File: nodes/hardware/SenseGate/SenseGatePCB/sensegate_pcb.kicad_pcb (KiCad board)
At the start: 2 copper layers, 110.1 x 110.1 mm, 0 parts

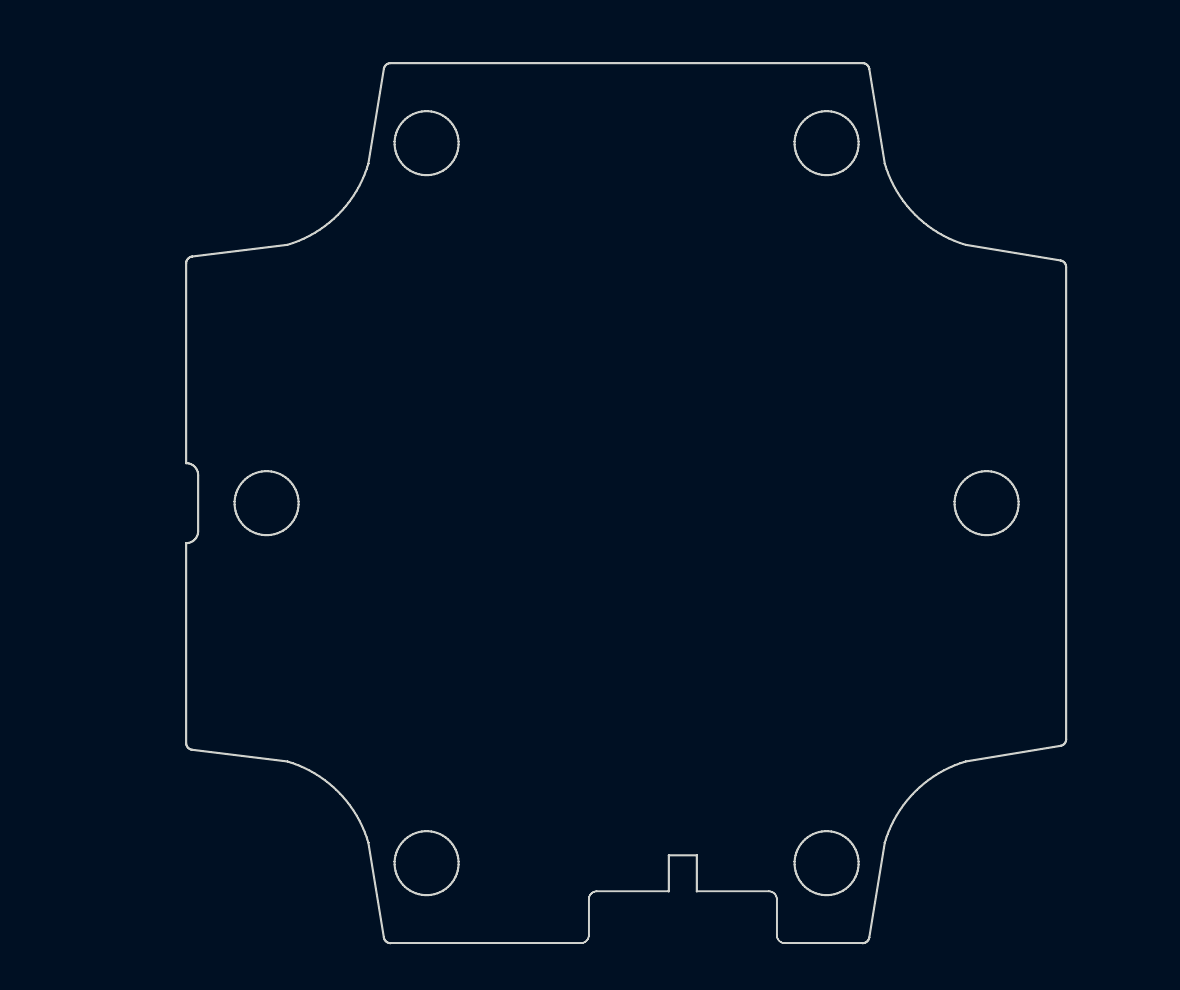
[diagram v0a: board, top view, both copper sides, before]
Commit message: added footprint with pads of sensemate to sensegate pcb
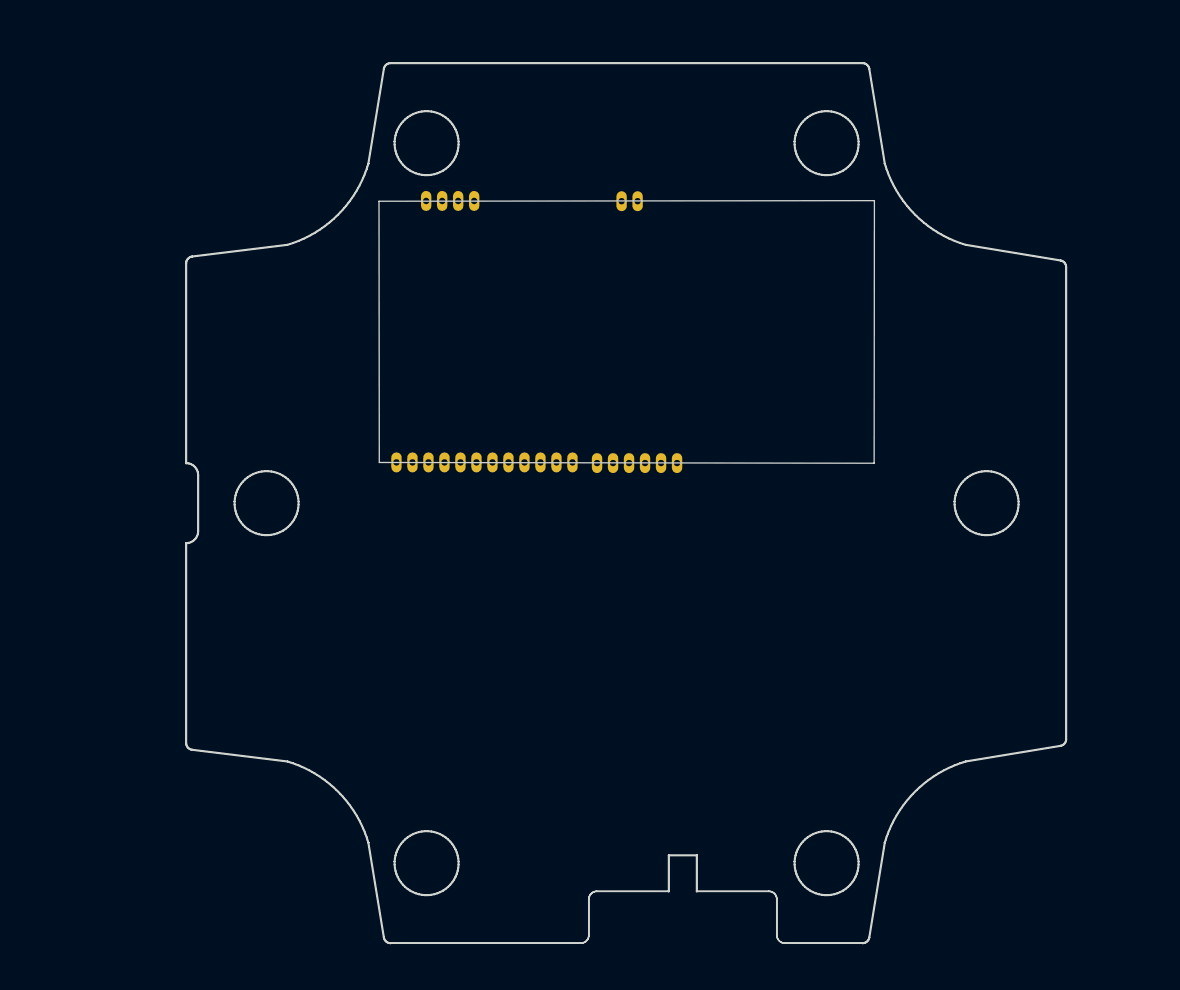
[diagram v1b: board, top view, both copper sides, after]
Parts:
- added J4: Conn_01x24_Pin, SenseGateLib:SenseMateInterface, F.Cu at (122.3, 54.5)

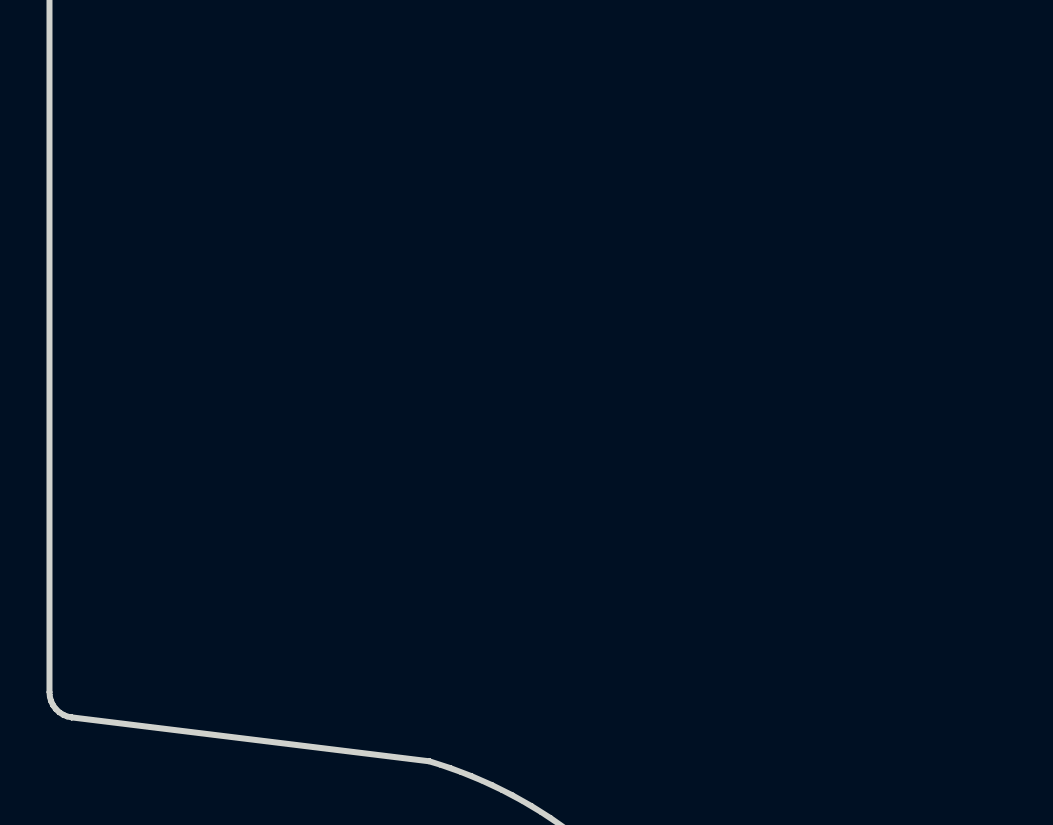
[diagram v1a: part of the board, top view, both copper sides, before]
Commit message: added solar boost converter footprint
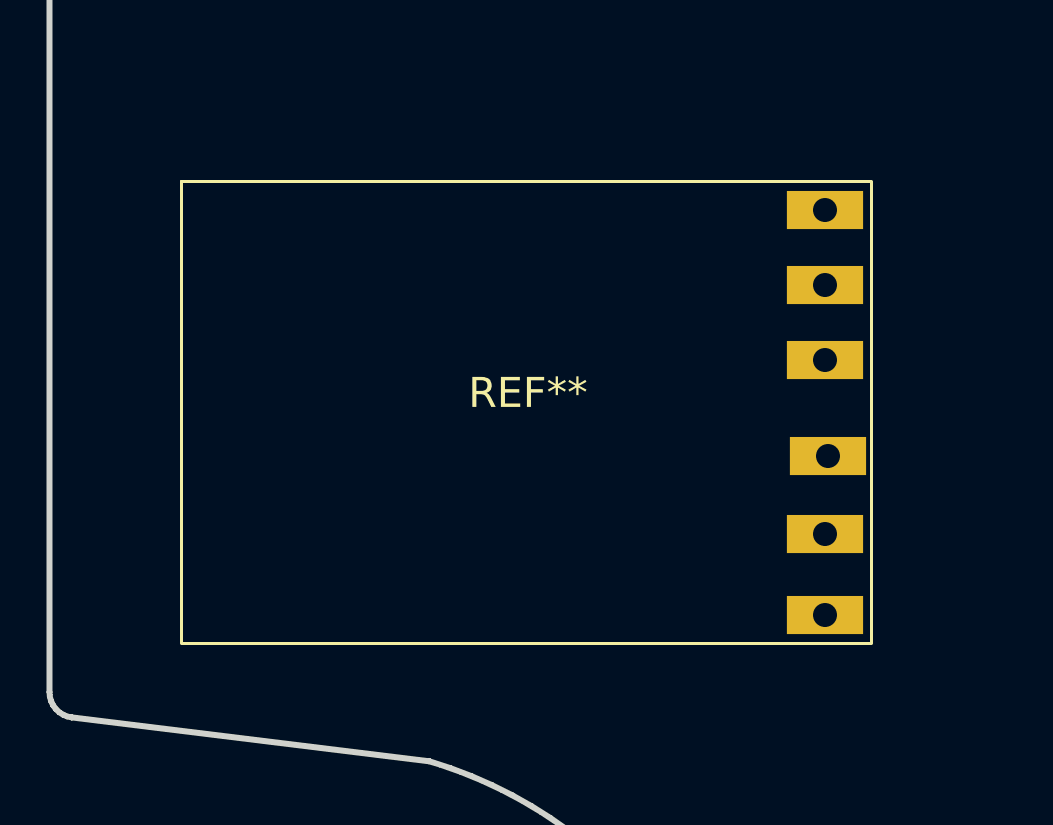
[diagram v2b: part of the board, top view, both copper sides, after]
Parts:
- added REF**: DD05CVSA, custom_dcdc_converters:DD05CVSA, F.Cu at (88.5, 114.5)
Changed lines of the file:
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@@
+		(embedded_fonts no)
+	)
+	(footprint "custom_dcdc_converters:DD05CVSA"
+		(layer "F.Cu")
+		(at 88.5 114.5)
+		(property "Reference" "REF**"
+			(at 0 -0.5 0)
+			(unlocked yes)
+			(layer "F.SilkS")
+			(effects
+				(font
+					(size 1 1)
+					(thickness 0.1)
+				)
+			)
+		)
+		(property "Value" "DD05CVSA"
+			(at 0 1 0)
+			(unlocked yes)
+			(layer "F.Fab")
+			(effects
+				(font
+					(size 1 1)
+					(thickness 0.15)
+				)
+			)
+		)
+		(property "Datasheet" ""
+			(at 0 0 0)
+			(unlocked yes)
+			(layer "F.Fab")
+			(hide yes)
+			(effects
+				(font
+					(size 1 1)
+					(thickness 0.15)
+				)
+			)
+		)
+		(property "Description" ""
+			(at 0 0 0)
+			(unlocked yes)
+			(layer "F.Fab")
+			(hide yes)
+			(effects
+				(font
+					(size 1 1)
+					(thickness 0.15)
+				)
+			)
+		)
+		(attr smd)
+		(duplicate_pad_numbers_are_jumpers no)
+		(fp_rect
+			(start -11.549748 -7.550756)
+			(end 11.450252 7.849244)
+			(stroke
+				(width 0.1)
+				(type default)
+			)
+			(fill no)
+			(layer "F.SilkS")
+		)
+		(fp_rect
+			(start -12 -8)
+			(end 11.9 8.3)
+			(stroke
+				(width 0.05)
+				(type default)
+			)
+			(fill no)
+			(layer "F.CrtYd")
+		)
+		(fp_text user "${REFERENCE}"
+			(at 0 2.5 0)
+			(unlocked yes)
+			(layer "F.Fab")
+			(effects
+				(font
+					(size 1 1)
+					(thickness 0.15)
+				)
+			)
+		)
+		(pad "1" thru_hole rect
+			(at 9.9 -6.6)
+			(size 2.54 1.27)
+			(drill 0.8)
+			(layers "*.Cu" "*.Mask")
+			(remove_unused_layers no)
+		)
+		(pad "2" thru_hole rect
+			(at 9.9 -4.1)
+			(size 2.54 1.27)
+			(drill 0.8)
+			(layers "*.Cu" "*.Mask")
+			(remove_unused_layers no)
+		)
+		(pad "3" thru_hole rect
+			(at 9.9 -1.6)
+			(size 2.54 1.27)
+			(drill 0.8)
+			(layers "*.Cu" "*.Mask")
+			(remove_unused_layers no)
+		)
+		(pad "4" thru_hole rect
+			(at 10 1.6)
+			(size 2.54 1.27)
+			(drill 0.8)
+			(layers "*.Cu" "*.Mask")
+			(remove_unused_layers no)
+		)
+		(pad "5" thru_hole rect
+			(at 9.9 4.2)
+			(size 2.54 1.27)
+			(drill 0.8)
+			(layers "*.Cu" "*.Mask")
+			(remove_unused_layers no)
+		)
+		(pad "6" thru_hole rect
+			(at 9.9 6.9)
+			(size 2.54 1.27)
+			(drill 0.8)
+			(layers "*.Cu" "*.Mask")
+			(remove_unused_layers no)
+		)
 		(embedded_fonts no)
 	)

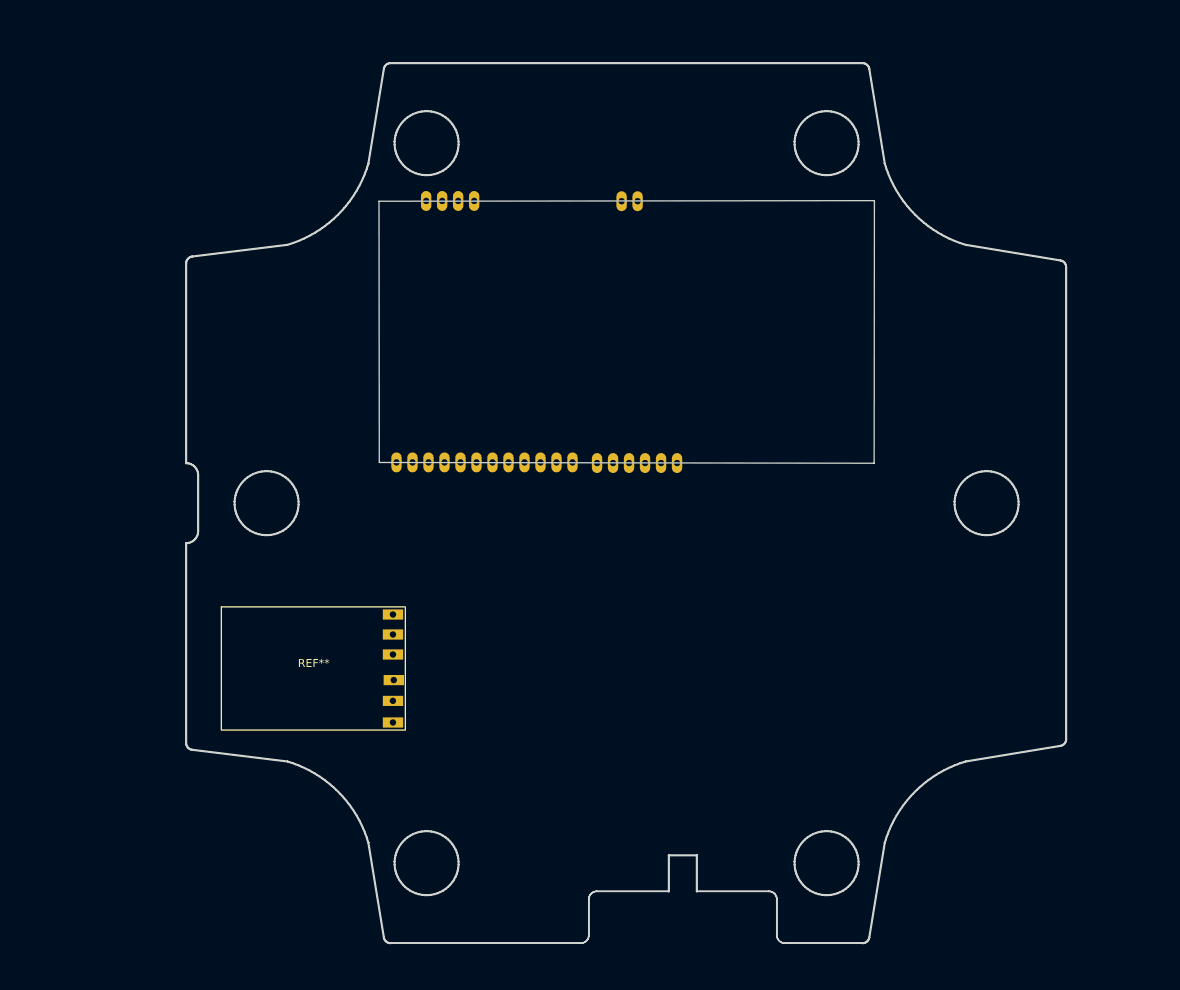
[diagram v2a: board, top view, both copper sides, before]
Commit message: added battery holder, jst terminals, and dcdc for inductive sensor
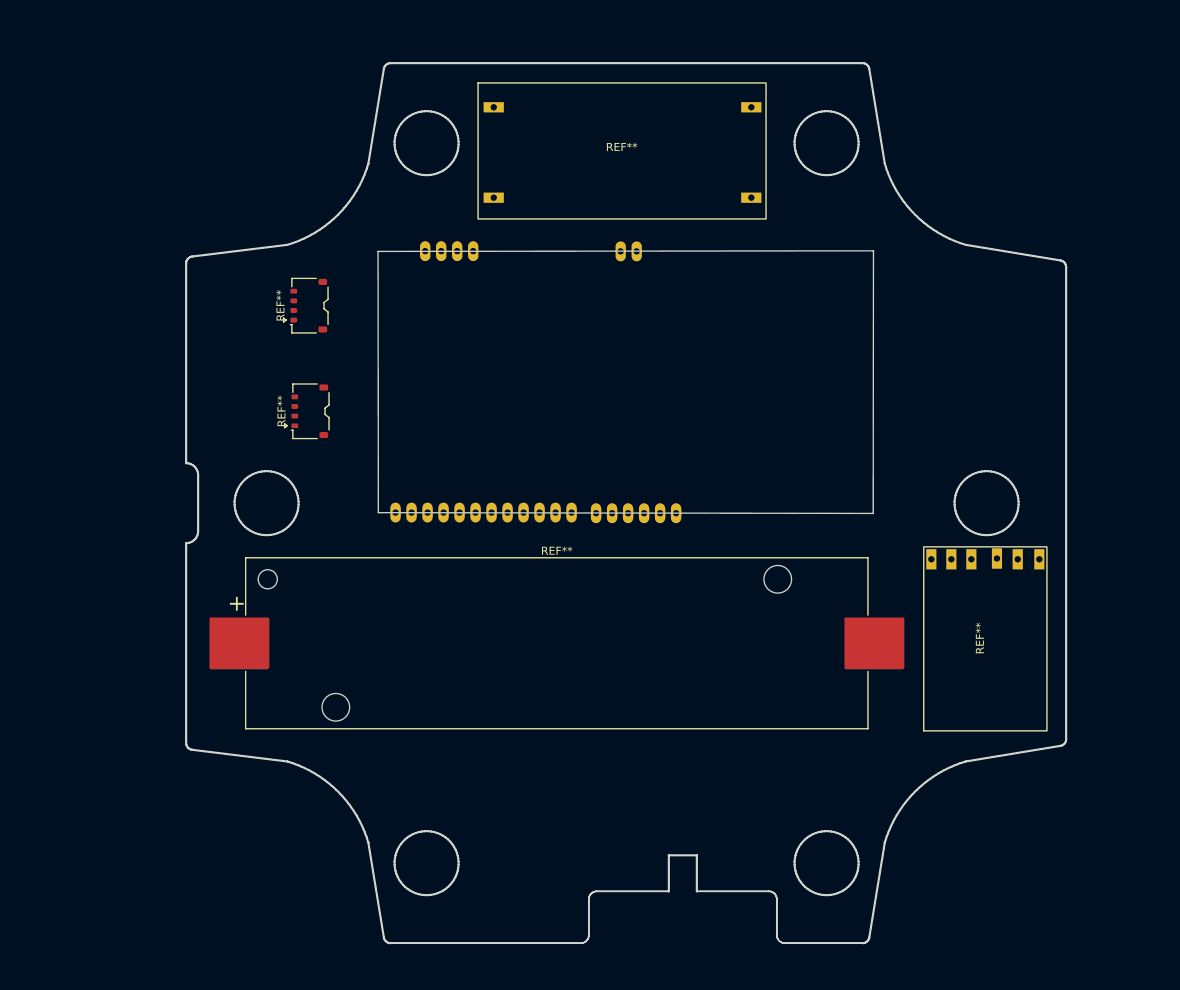
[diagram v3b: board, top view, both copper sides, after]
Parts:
- added REF**: JST_ACH_BM04B-ACHSS-A-GAN-ETF_1x04-1MP_P1.20mm_Vertical, Connector_JST:JST_ACH_BM04B-ACHSS-A-GAN-ETF_1x04-1MP_P1.20mm_Vertical, F.Cu at (87.9, 69.3)
- added REF**: BatteryHolder_Keystone_1042_1x18650, Battery:BatteryHolder_Keystone_1042_1x18650, F.Cu at (118.9, 111.5)
- added REF**: Solarbotics, custom_dcdc_converters:Solarbotics, F.Cu at (127.0, 50.0)
- added REF**: JST_ACH_BM04B-ACHSS-A-GAN-ETF_1x04-1MP_P1.20mm_Vertical, Connector_JST:JST_ACH_BM04B-ACHSS-A-GAN-ETF_1x04-1MP_P1.20mm_Vertical, F.Cu at (88.0, 82.5)
- moved REF** 83.9 mm to (172.3, 110.9), turned to 90 degrees
- moved J4 6.27 mm to (122.2, 60.8)

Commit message: wip schematic and pcb
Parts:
- removed REF** (x2): JST_ACH_BM04B-ACHSS-A-GAN-ETF_1x04-1MP_P1.20mm_Vertical, Connector_JST:JST_ACH_BM04B-ACHSS-A-GAN-ETF_1x04-1MP_P1.20mm_Vertical
- removed REF**: DD05CVSA, custom_dcdc_converters:DD05CVSA
- removed REF**: BatteryHolder_Keystone_1042_1x18650, Battery:BatteryHolder_Keystone_1042_1x18650
- removed REF**: Solarbotics, custom_dcdc_converters:Solarbotics
- added J5: Conn_01x04_Socket, Connector_JST:JST_PH_B4B-PH-K_1x04_P2.00mm_Vertical, F.Cu at (89.7, 106.1)
- added J6: Conn_01x04_Socket, Connector_JST:JST_PH_B4B-PH-K_1x04_P2.00mm_Vertical, F.Cu at (110.5, 108.9)
- added J7: Conn_01x04_Socket, Connector_JST:JST_PH_B4B-PH-K_1x04_P2.00mm_Vertical, F.Cu at (110.5, 115.5)
- added J8: Conn_01x04_Socket, Connector_JST:JST_PH_B4B-PH-K_1x04_P2.00mm_Vertical, F.Cu at (110.5, 122.0)
- added U1: DD05CVSA, custom_dcdc_converters:DD05CVSA, F.Cu at (171.4, 76.2)
- moved J4 0.14 mm to (122.3, 60.7)
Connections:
- J4 pad +3V3: (no net) -> unconnected-(J4-Pin_21-Pad+3V3)
- J4 pad Battery: (no net) -> unconnected-(J4-Pin_23-PadBattery)
- J4 pad GND: (no net) -> unconnected-(J4-Pin_16-PadGND)
- J4 pad P0.31_D16: (no net) -> unconnected-(J4-Pin_12-PadP0.31_D16)
- J4 pad VBAT: (no net) -> unconnected-(J4-Pin_24-PadVBAT)
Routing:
- added copper zone on F.Cu, net (none)

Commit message: sensegate pcb wip
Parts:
- added BT2: Battery, Connector_JST:JST_PH_S2B-PH-K_1x02_P2.00mm_Horizontal, F.Cu at (156.5, 100.3)
- added Q4: SS8050, Package_TO_SOT_SMD:SOT-23, F.Cu at (136.9, 117.5)
- added R3: R, Resistor_SMD:R_0805_2012Metric, F.Cu at (136.7, 121.2)
- moved U1 49.3 mm to (150.8, 120.9), turned to 90 degrees
- moved J8 19.5 mm to (118.5, 104.3), turned to 90 degrees
- moved J7 11.3 mm to (112.3, 104.3), turned to 90 degrees
- moved J5 10.2 mm to (99.7, 104.2), turned to 90 degrees
- moved J6 6.58 mm to (105.9, 104.2), turned to 90 degrees
- moved J4 5.27 mm to (123.1, 55.5)
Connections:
- J4 pad +3V3: unconnected-(J4-Pin_21-Pad+3V3) -> +3V3
- J4 pad GND: unconnected-(J4-Pin_16-PadGND) -> GND
- J4 pad VBAT: unconnected-(J4-Pin_24-PadVBAT) -> VBAT
- J5 pad 1: testt -> unconnected-(J5-Pin_1-Pad1)
- U1 pad 5: unconnected-(U1-GND-Pad5) -> GND
- U1 pad 6: unconnected-(U1-VOUT-Pad6) -> VBAT

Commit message: schematic done
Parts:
- added J3: Conn_01x02_Socket, Connector_JST:JST_PH_B2B-PH-K_1x02_P2.00mm_Vertical, F.Cu at (144.3, 104.7)
- added J9: Conn_01x04_Socket, Connector_JST:JST_PH_B4B-PH-K_1x04_P2.00mm_Vertical, F.Cu at (123.9, 112.5)
- added R10: R, Resistor_SMD:R_0805_2012Metric, F.Cu at (116.9, 101.7)
- added R11: R, Resistor_SMD:R_0805_2012Metric, F.Cu at (119.7, 101.7)
- added R12: R, Resistor_SMD:R_0805_2012Metric, F.Cu at (110.8, 101.8)
- added R13: R, Resistor_SMD:R_0805_2012Metric, F.Cu at (113.4, 101.8)
- added R14: R, Resistor_SMD:R_0805_2012Metric, F.Cu at (104.5, 101.5)
- added R15: R, Resistor_SMD:R_0805_2012Metric, F.Cu at (106.9, 101.5)
- added R4: R, Resistor_SMD:R_0805_2012Metric, F.Cu at (142.8, 98.9)
- added R5: R, Resistor_SMD:R_0805_2012Metric, F.Cu at (138.6, 98.9)
- added R6: R, Resistor_SMD:R_0805_2012Metric, F.Cu at (100.9, 93.3)
- added R7: R, Resistor_SMD:R_0805_2012Metric, F.Cu at (97.0, 93.2)
- added R8: R, Resistor_SMD:R_0805_2012Metric, F.Cu at (123.0, 101.7)
- added R9: R, Resistor_SMD:R_0805_2012Metric, F.Cu at (125.6, 101.7)
- added U2: mt3608_dcdc_converter, custom_dcdc_converters:MT3608_solarbotics, F.Cu at (118.3, 125.4)
- moved R3 14.6 mm to (135.6, 106.6), turned to 90 degrees
- moved Q4 12.2 mm to (131.9, 106.3), turned to 90 degrees
- moved J5 8.20 mm to (99.0, 112.4)
- moved J6 8.20 mm to (105.2, 112.4)
- moved J7 8.20 mm to (111.6, 112.5)
- moved J8 8.20 mm to (117.9, 112.5)
- moved BT2 4.96 mm to (154.3, 104.8), turned to 180 degrees
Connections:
- J4 pad P0.04_A4_D4_/_SDA: unconnected-(J4-9-PadP0.04_A4_D4_/_SDA) -> reed_sw_04_measure
- J4 pad P0.05_A5_D5_/_SCL: unconnected-(J4-Pin_11-PadP0.05_A5_D5_/_SCL) -> MON_SOLAR
- J5 pad 2: GND -> GND_IS
- J5 pad 4: IS_ADC -> Net-(J5-Pin_4)
- J6 pad 2: unconnected-(J6-Pin_2-Pad2) -> GND
- J6 pad 3: reed_sw_02_measure -> +3V3
- J6 pad 4: +3V3 -> reed_sw_02_measure
- J7 pad 2: unconnected-(J7-Pin_2-Pad2) -> GND
- J7 pad 3: reed_sw_03_measure -> +3V3
- J7 pad 4: +3V3 -> reed_sw_03_measure
- J8 pad 2: unconnected-(J8-Pin_2-Pad2) -> GND
- J8 pad 3: reed_sw_01_measure -> +3V3
- J8 pad 4: +3V3 -> reed_sw_01_measure
- Q4 pad 2: unconnected-(Q4-E-Pad2) -> Net-(Q4-E)
- Q4 pad 3: unconnected-(Q4-C-Pad3) -> VBAT
- U1 pad 3: Net-(J9-Pin_2) -> VBAT
- U1 pad 4: Net-(J9-Pin_1) -> GND
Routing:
- added copper zone on B.Cu, net GND
- added copper zone on F.Cu, net GND
- removed copper zone on F.Cu, net (none)
